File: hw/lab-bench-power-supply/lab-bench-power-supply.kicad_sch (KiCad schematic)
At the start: 9 parts, among them Q1 TIP42C, Q2 Q_NPN, Q3 BC856BS

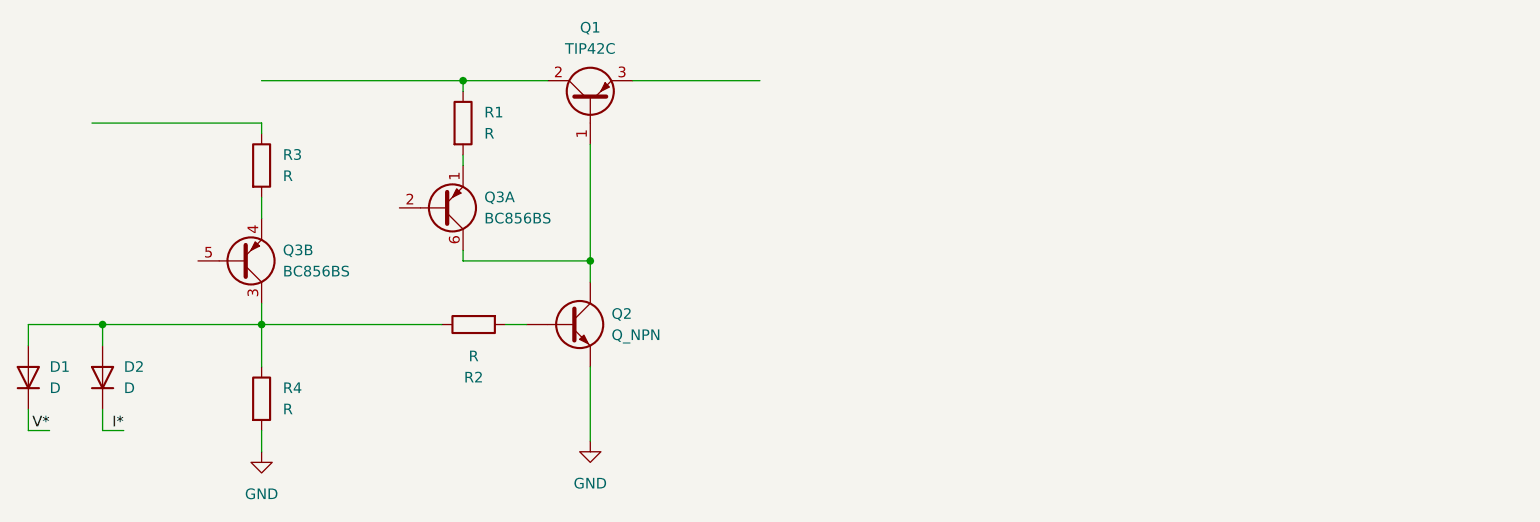
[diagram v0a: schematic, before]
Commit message: Added Simetrix / Simplis dual phase buck design
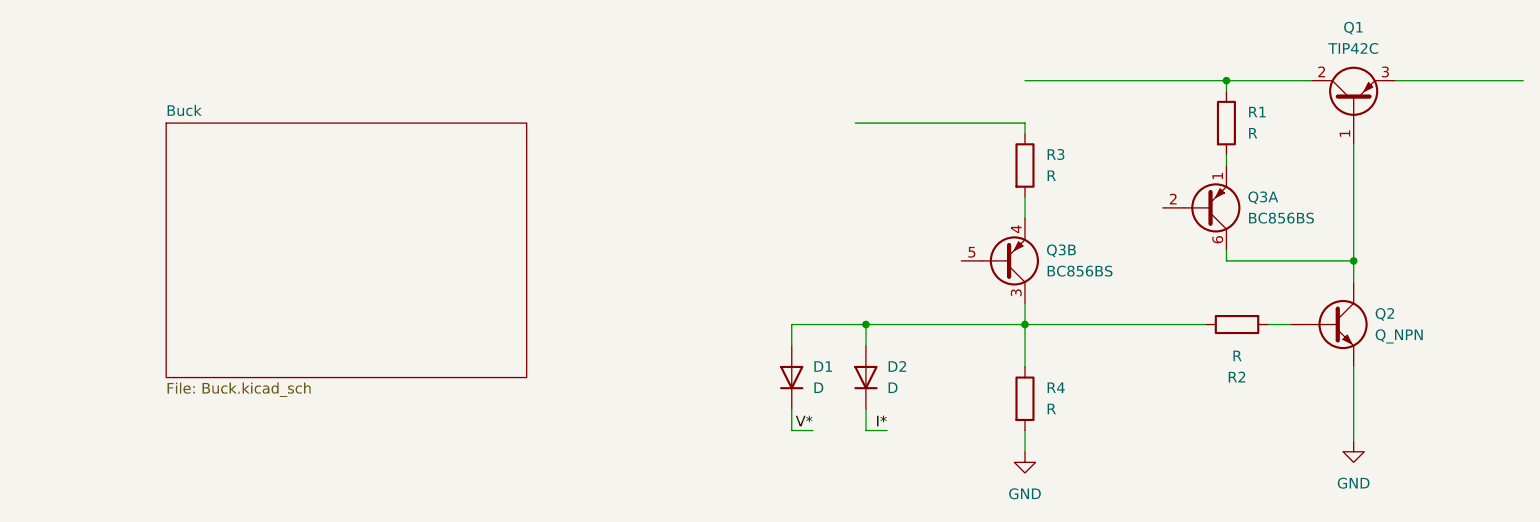
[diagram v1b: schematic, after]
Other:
- added sheet Buck (Buck.kicad_sch)
- moved on the sheet: D1, D2, Q1, Q2, Q3A, Q3B, R1, R2, R3, R4
